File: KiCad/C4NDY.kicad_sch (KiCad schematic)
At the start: 42 parts, among them J1 Conn_01x08, J2 Conn_01x07, J3 Conn_01x05, J4 5077CR-16SMC2-BK-TR, J5 Conn_01x06, J6 Conn_01x08, J7 FTSH-105-01-L-DV-K, SW1 SKRPABE010, SW2 SKRPABE010, U1 MIC39100-3.3WS, U2 IS66WVS2M8BLL, U3 STM32G4A1CETx, X1 SG-310SCF

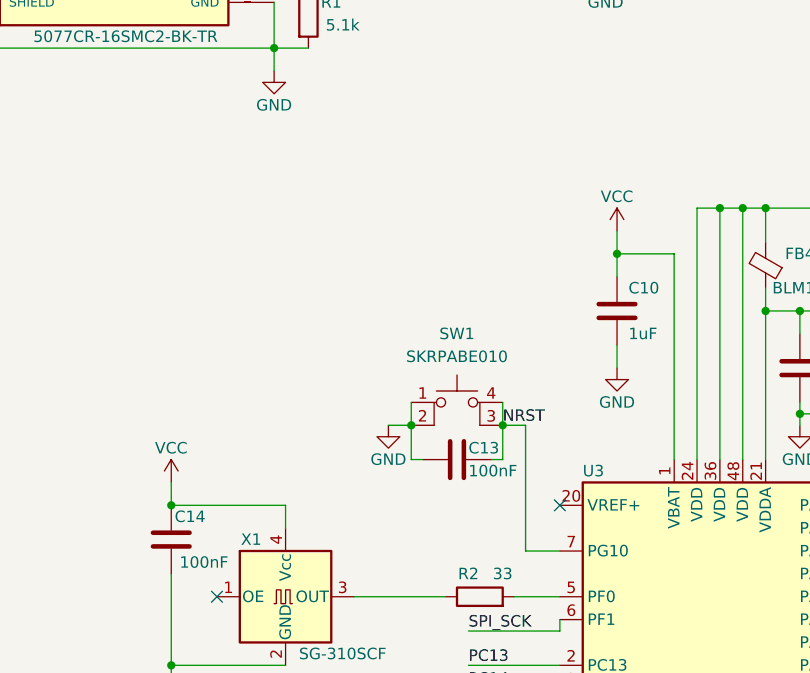
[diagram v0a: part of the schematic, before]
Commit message: VrefをVCCに接続し、マイコン周辺の部品配置と配線を修正
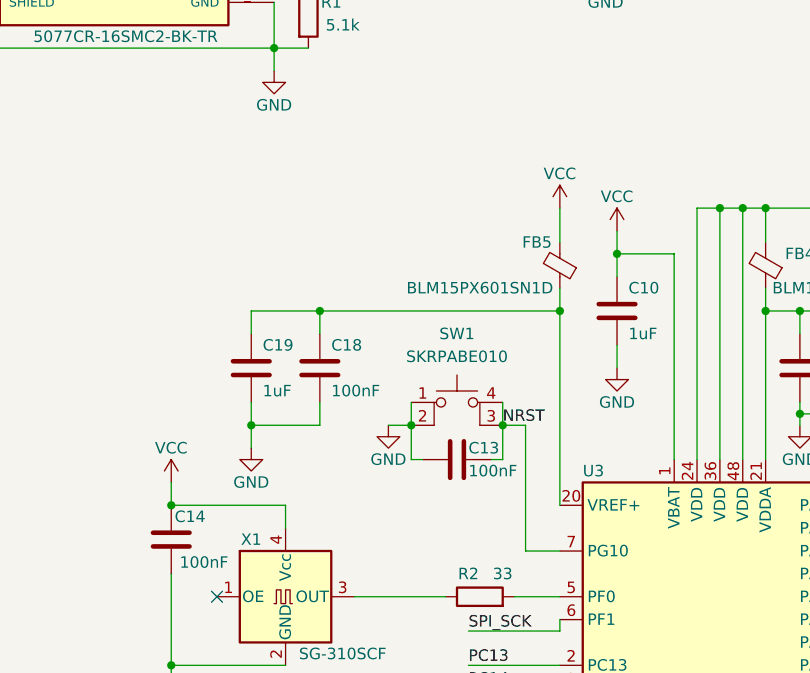
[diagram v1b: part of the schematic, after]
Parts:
- added C18: 100nF, Capacitor_SMD:C_0402_1005Metric, symbol Device:C
- added C19: 1uF, Capacitor_SMD:C_0402_1005Metric, symbol Device:C
- added FB5: BLM15PX601SN1D, Inductor_SMD:L_0402_1005Metric, symbol Device:FerriteBead_Small
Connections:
- net GND: now also C18.2, C19.2
- net VCC: now also FB5.2
- net at U3.20 (VREF+): now also C18.1, C19.1, FB5.1
- no-connect marks 8 -> 7
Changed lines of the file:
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@@
   (junction (at 212.09 124.46) (diameter 0) (color 0 0 0 0)
   )
+  (junction (at 87.63 87.63) (diameter 0) (color 0 0 0 0)
+  )
   (junction (at 173.99 137.16) (diameter 0) (color 0 0 0 0)
   )
@@
   (junction (at 114.3 99.06) (diameter 0) (color 0 0 0 0)
   )
+  (junction (at 53.34 100.33) (diameter 0) (color 0 0 0 0)
+  )
   (junction (at 140.97 35.56) (diameter 0) (color 0 0 0 0)
   )
@@
   )
   (junction (at 139.7 88.9) (diameter 0) (color 0 0 0 0)
+  )
+  (junction (at 60.96 87.63) (diameter 0) (color 0 0 0 0)
   )
   (junction (at 92.71 46.99) (diameter 0) (color 0 0 0 0)
@@
   (no_connect (at 259.08 128.27))
   (no_connect (at 55.88 40.64))
-  (no_connect (at 87.63 109.22))
   (no_connect (at 49.53 119.38))
   (no_connect (at 246.38 133.35))
@@
     (stroke (width 0) (type default))
   )
+  (wire (pts (xy 87.63 87.63) (xy 87.63 109.22))
+    (stroke (width 0) (type default))
+  )
   (wire (pts (xy 120.65 142.24) (xy 123.19 142.24))
     (stroke (width 0) (type default))
@@
     (stroke (width 0) (type default))
   )
+  (wire (pts (xy 53.34 90.17) (xy 53.34 87.63))
+    (stroke (width 0) (type default))
+  )
   (wire (pts (xy 83.82 114.3) (xy 87.63 114.3))
     (stroke (width 0) (type default))
@@
     (stroke (width 0) (type default))
   )
+  (wire (pts (xy 53.34 97.79) (xy 53.34 100.33))
+    (stroke (width 0) (type default))
+  )
   (wire (pts (xy 107.95 76.2) (xy 107.95 104.14))
     (stroke (width 0) (type default))
@@
     (stroke (width 0) (type default))
   )
+  (wire (pts (xy 60.96 100.33) (xy 53.34 100.33))
+    (stroke (width 0) (type default))
+  )
   (wire (pts (xy 60.96 168.91) (xy 60.96 171.45))
     (stroke (width 0) (type default))
@@
     (stroke (width 0) (type default))
   )
+  (wire (pts (xy 60.96 90.17) (xy 60.96 87.63))
+    (stroke (width 0) (type default))
+  )
   (wire (pts (xy 227.33 31.75) (xy 237.49 31.75))
     (stroke (width 0) (type default))
@@
     (stroke (width 0) (type default))
   )
+  (wire (pts (xy 87.63 85.09) (xy 87.63 87.63))
+    (stroke (width 0) (type default))
+  )
   (wire (pts (xy 76.2 157.48) (xy 87.63 157.48))
     (stroke (width 0) (type default))
@@
     (stroke (width 0) (type default))
   )
+  (wire (pts (xy 87.63 80.01) (xy 87.63 76.2))
+    (stroke (width 0) (type default))
+  )
   (wire (pts (xy 110.49 87.63) (xy 110.49 104.14))
     (stroke (width 0) (type default))
@@
     (stroke (width 0) (type default))
   )
+  (wire (pts (xy 53.34 87.63) (xy 60.96 87.63))
+    (stroke (width 0) (type default))
+  )
+  (wire (pts (xy 53.34 100.33) (xy 53.34 102.87))
+    (stroke (width 0) (type default))
+  )
   (wire (pts (xy 60.96 173.99) (xy 62.23 173.99))
     (stroke (width 0) (type default))
@@
     (stroke (width 0) (type default))
   )
+  (wire (pts (xy 60.96 87.63) (xy 87.63 87.63))
+    (stroke (width 0) (type default))
+  )
   (wire (pts (xy 139.7 76.2) (xy 139.7 78.74))
     (stroke (width 0) (type default))
@@
   )
   (wire (pts (xy 77.47 154.94) (xy 87.63 154.94))
+    (stroke (width 0) (type default))
+  )
+  (wire (pts (xy 60.96 97.79) (xy 60.96 100.33))
     (stroke (width 0) (type default))
   )
@@
         (path "/868f46d4-ce7a-4a96-bb33-8a76e5eb710a"
           (reference "#PWR07") (unit 1)
+        )
+      )
+    )
+  )
+  (symbol (lib_id "Device:FerriteBead_Small") (at 87.63 82.55 180) (unit 1)
+    (in_bom yes) (on_board yes) (dnp no)
+    (property "Reference" "FB5" (at 85.09 80.01 0)
+      (effects (font (size 1.27 1.27)))
+    )
+    (property "Value" "BLM15PX601SN1D" (at 78.74 85.09 0)
+      (effects (font (size 1.27 1.27)))
+    )
+    (property "Footprint" "Inductor_SMD:L_0402_1005Metric" (at 89.408 82.55 90)
+      (effects (font (size 1.27 1.27)) hide)
+    )
+    (property "Datasheet" "~" (at 87.63 82.55 0)
+      (effects (font (size 1.27 1.27)) hide)
+    )
+    (pin "1")
+    (pin "2")
+    (instances
+      (project "C4NDY"
+        (path "/868f46d4-ce7a-4a96-bb33-8a76e5eb710a"
+          (reference "FB5") (unit 1)
         )
       )
@@
         (path "/868f46d4-ce7a-4a96-bb33-8a76e5eb710a"
           (reference "#PWR05") (unit 1)
+        )
+      )
+    )
+  )
+  (symbol (lib_id "Device:C") (at 53.34 93.98 0) (unit 1)
+    (in_bom yes) (on_board yes) (dnp no)
+    (property "Reference" "C19" (at 54.61 91.44 0)
+      (effects (font (size 1.27 1.27)) (justify left))
+    )
+    (property "Value" "1uF" (at 54.61 96.52 0)
+      (effects (font (size 1.27 1.27)) (justify left))
+    )
+    (property "Footprint" "Capacitor_SMD:C_0402_1005Metric" (at 54.3052 97.79 0)
+      (effects (font (size 1.27 1.27)) hide)
+    )
+    (property "Datasheet" "~" (at 53.34 93.98 0)
+      (effects (font (size 1.27 1.27)) hide)
+    )
+    (pin "1")
+    (pin "2")
+    (instances
+      (project "C4NDY"
+        (path "/868f46d4-ce7a-4a96-bb33-8a76e5eb710a"
+          (reference "C19") (unit 1)
         )
       )
@@
         (path "/868f46d4-ce7a-4a96-bb33-8a76e5eb710a"
           (reference "J4") (unit 1)
+        )
+      )
+    )
+  )
+  (symbol (lib_id "power:VCC") (at 87.63 76.2 0) (unit 1)
+    (in_bom yes) (on_board yes) (dnp no)
+    (property "Reference" "#PWR035" (at 87.63 80.01 0)
+      (effects (font (size 1.27 1.27)) hide)
+    )
+    (property "Value" "VCC" (at 87.63 72.39 0)
+      (effects (font (size 1.27 1.27)))
+    )
+    (property "Footprint" "" (at 87.63 76.2 0)
+      (effects (font (size 1.27 1.27)) hide)
+    )
+    (property "Datasheet" "" (at 87.63 76.2 0)
+      (effects (font (size 1.27 1.27)) hide)
+    )
+    (pin "1")
+    (instances
+      (project "C4NDY"
+        (path "/868f46d4-ce7a-4a96-bb33-8a76e5eb710a"
+          (reference "#PWR035") (unit 1)
         )
       )
@@
     )
   )
+  (symbol (lib_id "Device:C") (at 60.96 93.98 0) (unit 1)
+    (in_bom yes) (on_board yes) (dnp no)
+    (property "Reference" "C18" (at 62.23 91.44 0)
+      (effects (font (size 1.27 1.27)) (justify left))
+    )
+    (property "Value" "100nF" (at 62.23 96.52 0)
+      (effects (font (size 1.27 1.27)) (justify left))
+    )
+    (property "Footprint" "Capacitor_SMD:C_0402_1005Metric" (at 61.9252 97.79 0)
+      (effects (font (size 1.27 1.27)) hide)
+    )
+    (property "Datasheet" "~" (at 60.96 93.98 0)
+      (effects (font (size 1.27 1.27)) hide)
+    )
+    (pin "1")
+    (pin "2")
+    (instances
+      (project "C4NDY"
+        (path "/868f46d4-ce7a-4a96-bb33-8a76e5eb710a"
+          (reference "C18") (unit 1)
+        )
+      )
+    )
+  )
   (symbol (lib_id "power:VDD") (at 92.71 33.02 0) (unit 1)
     (in_bom yes) (on_board yes) (dnp no) (fields_autoplaced)
@@
         )
       )
+    )
+  )
+  (symbol (lib_id "power:GND") (at 53.34 102.87 0) (unit 1)
+    (in_bom yes) (on_board yes) (dnp no)
+    (property "Reference" "#PWR034" (at 53.34 109.22 0)
+      (effects (font (size 1.27 1.27)) hide)
+    )
+    (property "Value" "GND" (at 53.34 106.68 0)
+      (effects (font (size 1.27 1.27)))
+    )
+    (property "Footprint" "" (at 53.34 102.87 0)
+      (effects (font (size 1.27 1.27)) hide)
+    )
+    (property "Datasheet" "" (at 53.34 102.87 0)
+      (effects (font (size 1.27 1.27)) hide)
+    )
+    (pin "1")
+    (instances
+      (project "C4NDY"
+        (path "/868f46d4-ce7a-4a96-bb33-8a76e5eb710a"
+          (reference "#PWR034") (unit 1)
+        )
+      )
